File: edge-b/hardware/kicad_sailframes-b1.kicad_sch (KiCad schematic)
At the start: 79 parts, among them J1 Conn_01x15, J10 I2C_EXP1, J11 I2C_EXP2, J12 I2C_EXP3, J13 GPIO_EXP, J14 UART_DBG, J15 J_AUX, J16 GNSS_DBG, J17 LATCH_DBG, J2 JST_PH_BAT, J3 U.FL, J4 Conn_01x15, J5 MICROSD, J8 BNO085_DIRECT_SOLDER, J9 HOSYOND_3.5_TFT, U1 LC29HEAMD, U2 TP4056, U3 MT3608, U4 ESP32_DEVKIT_V1

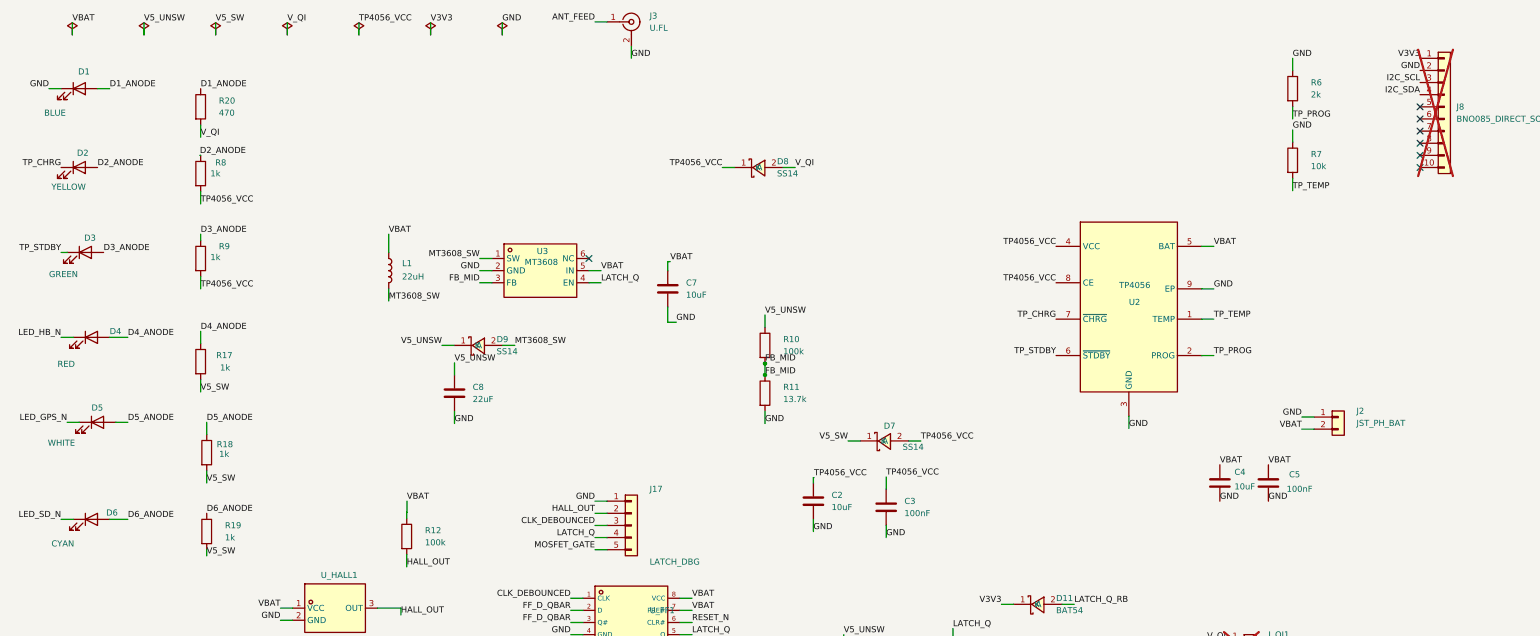
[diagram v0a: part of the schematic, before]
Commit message: B1: D6 cyan->blue, finalize JLC assembly BOM
- D6 LED cyan -> blue (C99290, same as D1) + filled its missing LCSC
- BOM finalized with tier-optimized parts (10k=C25804 Basic, TP4056=C16581,
  yellow=C89811, green=C99289, J1/J4=C2932676); deduped designators
  -> bom-jlcpcb-clean.csv (plugin had a duplicate-designator bug)
- NOTE: U_FF1 still C70285 (DCU) in schematic; correct part is
  SN74LVC1G74DCTR / SM8 = C840104 (fixed in JLC order, update schematic next)

Co-Authored-By: Claude Opus 4.8 (1M context) <noreply@anthropic.com>
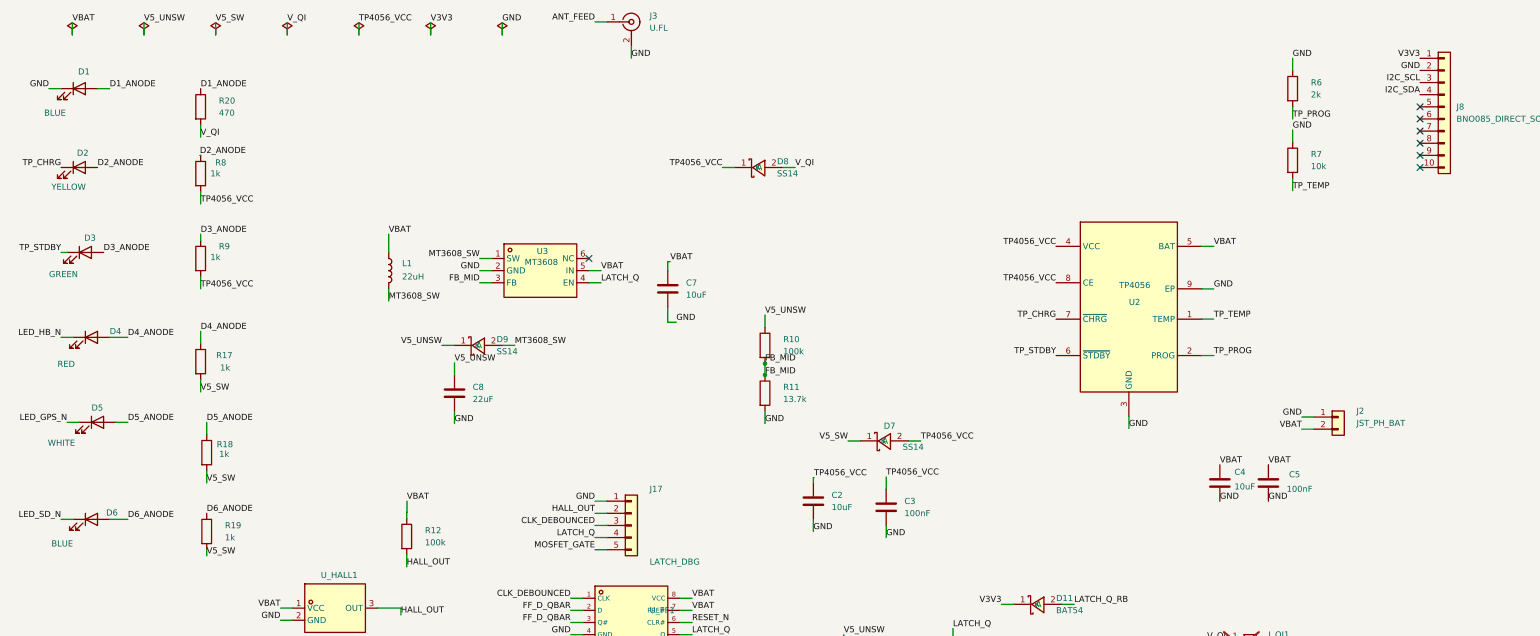
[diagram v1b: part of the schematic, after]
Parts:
- D6: value CYAN -> BLUE; LCSC Part # (none) -> C99290
- J8: now fitted; now in the parts list
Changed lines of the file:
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@@
 			)
 		)
-		(property "Value" "CYAN"
+		(property "Value" "BLUE"
 			(at 20.828 127 0)
 			(show_name no)
@@
 		(property "Description" ""
 			(at 29.21 121.92 0)
+			(hide yes)
+			(show_name no)
+			(do_not_autoplace no)
+			(effects
+				(font
+					(size 1.27 1.27)
+				)
+			)
+		)
+		(property "LCSC Part #" "C99290"
+			(at 20.828 127 0)
 			(hide yes)
 			(show_name no)
@@
 		(body_style 1)
 		(exclude_from_sim no)
-		(in_bom no)
+		(in_bom yes)
 		(on_board yes)
-		(in_pos_files no)
-		(dnp yes)
+		(in_pos_files yes)
+		(dnp no)
 		(fields_autoplaced yes)
 		(property "Reference" "J8"

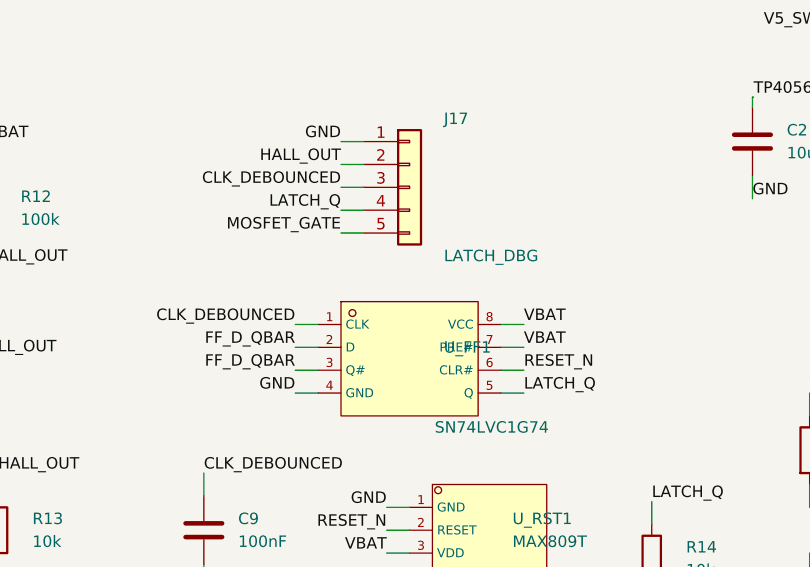
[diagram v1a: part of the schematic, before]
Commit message: edge-b/B1 hardware: KiCad PCB/schematic update + regenerated production files
- U_FF1 footprint swap: drop the mislabeled SM8 footprint and add the correct
  SN74LVC1G74 TSSOP8 footprint (C458768) to the B1_JLC library
- Updated kicad_sailframes-b1 PCB + schematic
- Regenerated production deliverables: gerbers zip, BOM, IPC netlist, CPL
  positions, and the JLCPCB fab BOM

Co-Authored-By: Claude Opus 4.8 (1M context) <noreply@anthropic.com>
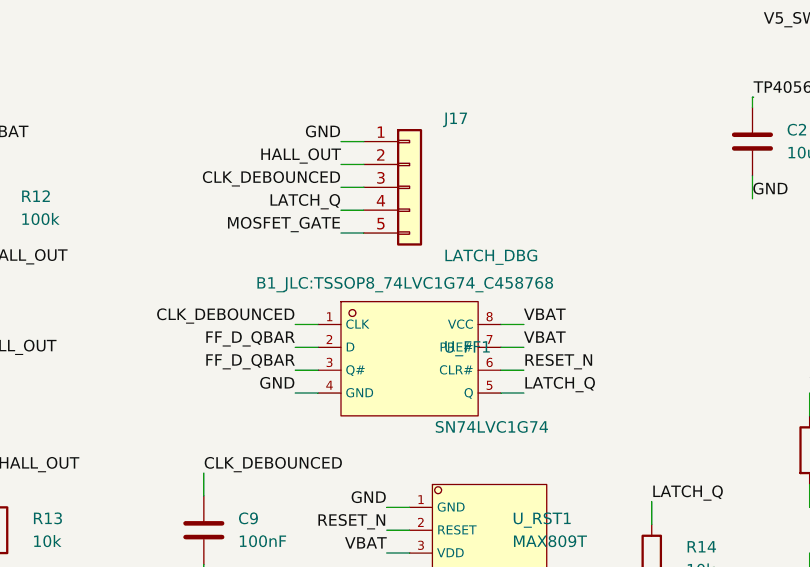
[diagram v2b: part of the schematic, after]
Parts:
- D2: LCSC Part # C125093 -> C89811
- D3: LCSC Part # C125093 -> C99289
- J1, J4: LCSC Part # (none) -> C2932676
- J10, J11, J12, J14, J16: LCSC Part # C2337 -> C5116483
- J13, J17: LCSC Part # C2337 -> C5156614
- J15: LCSC Part # C2337 -> C32713272
- J8: LCSC Part # (none) -> C57369
- J9: LCSC Part # C2337 -> C57369
- R13, R14, R16, R23, R24, R25, R26, R27, R28, R7: LCSC Part # C15401 -> C25804
- U2: LCSC Part # C382139 -> C16581
- U_FF1: footprint B1_JLC:VSSOP-8_DCU_2.3x2mm_P0.65mm -> B1_JLC:TSSOP8_74LVC1G74_C458768; LCSC Part # C70285 -> C458768
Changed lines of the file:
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@@
 			)
 		)
-		(property "LCSC Part #" "C2337"
+		(property "LCSC Part #" "C5116483"
 			(at 0 0 0)
 			(hide yes)
@@
 			)
 		)
-		(property "LCSC Part #" "C2337"
+		(property "LCSC Part #" "C5156614"
 			(at -107.76 -96.81 0)
 			(hide yes)
@@
 			)
 		)
-		(property "LCSC Part #" "C15401"
+		(property "LCSC Part #" "C25804"
 			(at 0 0 0)
 			(hide yes)
@@
 			)
 		)
-		(property "LCSC Part #" "C2337"
+		(property "LCSC Part #" "C57369"
 			(at 0 0 0)
 			(hide yes)
@@
 			)
 		)
-		(property "LCSC Part #" "C125093"
+		(property "LCSC Part #" "C89811"
 			(at -188.54 -37.24 0)
 			(hide yes)
@@
 			)
 		)
+		(property "LCSC Part #" "C2932676"
+			(at 351.79 114.3 0)
+			(hide yes)
+			(show_name no)
+			(do_not_autoplace no)
+			(effects
+				(font
+					(size 1.27 1.27)
+				)
+			)
+		)
 		(property "Datasheet" ""
 			(at 351.79 114.3 0)
@@
 			)
 		)
-		(property "LCSC Part #" "C15401"
+		(property "LCSC Part #" "C25804"
 			(at 0 0 0)
 			(hide yes)
@@
 			)
 		)
-		(property "LCSC Part #" "C2337"
+		(property "LCSC Part #" "C5116483"
 			(at 0 0 0)
 			(hide yes)
@@
 			)
 		)
-		(property "LCSC Part #" "C2337"
+		(property "LCSC Part #" "C5116483"
 			(at 46.99 78.74 0)
 			(hide yes)
@@
 			)
 		)
-		(property "LCSC Part #" "C15401"
+		(property "LCSC Part #" "C25804"
 			(at 0 0 0)
 			(hide yes)
@@
 			)
 		)
-		(property "LCSC Part #" "C15401"
+		(property "LCSC Part #" "C25804"
 			(at 0 0 0)
 			(hide yes)
@@
 			)
 		)
-		(property "Footprint" "B1_JLC:VSSOP-8_DCU_2.3x2mm_P0.65mm"
-			(at 142.24 142.24 0)
-			(hide yes)
+		(property "Footprint" "B1_JLC:TSSOP8_74LVC1G74_C458768"
+			(at 141.732 133.858 0)
 			(show_name no)
 			(do_not_autoplace no)
@@
 			)
 		)
-		(property "LCSC Part #" "C70285"
+		(property "LCSC Part #" "C458768"
 			(at 2.03 1.74 0)
 			(hide yes)
@@
 			)
 		)
-		(property "LCSC Part #" "C15401"
+		(property "LCSC Part #" "C25804"
 			(at 0 0 0)
 			(hide yes)
@@
 			)
 		)
-		(property "LCSC Part #" "C382139"
+		(property "LCSC Part #" "C16581"
 			(at 6.35 -5.08 0)
 			(hide yes)
@@
 			)
 		)
-		(property "LCSC Part #" "C2337"
+		(property "LCSC Part #" "C5116483"
 			(at 46.99 78.74 0)
 			(hide yes)
@@
 			)
 		)
+		(property "LCSC Part #" "C2932676"
+			(at 393.7 114.3 0)
+			(hide yes)
+			(show_name no)
+			(do_not_autoplace no)
+			(effects
+				(font
+					(size 1.27 1.27)
+				)
+			)
+		)
 		(property "Datasheet" ""
 			(at 393.7 114.3 0)
@@
 			)
 		)
-		(property "LCSC Part #" "C2337"
+		(property "LCSC Part #" "C32713272"
 			(at 0 0 0)
 			(hide yes)
@@
 			)
 		)
+		(property "LCSC Part #" "C57369"
+			(at 312.42 35.56 0)
+			(hide yes)
+			(show_name no)
+			(do_not_autoplace no)
+			(effects
+				(font
+					(size 1.27 1.27)
+				)
+			)
+		)
 		(property "Datasheet" ""
 			(at 312.42 35.56 0)
@@
 			)
 		)
-		(property "LCSC Part #" "C15401"
+		(property "LCSC Part #" "C25804"
 			(at 0 0 0)
 			(hide yes)
@@
 			)
 		)
-		(property "LCSC Part #" "C2337"
+		(property "LCSC Part #" "C5156614"
 			(at 46.99 78.74 0)
 			(hide yes)
@@
 			)
 		)
-		(property "LCSC Part #" "C15401"
+		(property "LCSC Part #" "C25804"
 			(at 0 0 0)
 			(hide yes)
@@
 			)
 		)
-		(property "LCSC Part #" "C15401"
+		(property "LCSC Part #" "C25804"
 			(at 10.46 -43.75 0)
 			(hide yes)
@@
 			)
 		)
-		(property "LCSC Part #" "C15401"
+		(property "LCSC Part #" "C25804"
 			(at 0 0 0)
 			(hide yes)
@@
 			)
 		)
-		(property "LCSC Part #" "C15401"
+		(property "LCSC Part #" "C25804"
 			(at 0 0 0)
 			(hide yes)
@@
 			)
 		)
-		(property "LCSC Part #" "C125093"
+		(property "LCSC Part #" "C99289"
 			(at -187.27 -4.46 0)
 			(hide yes)
@@
 			)
 		)
-		(property "LCSC Part #" "C2337"
+		(property "LCSC Part #" "C5116483"
 			(at 0 0 0)
 			(hide yes)

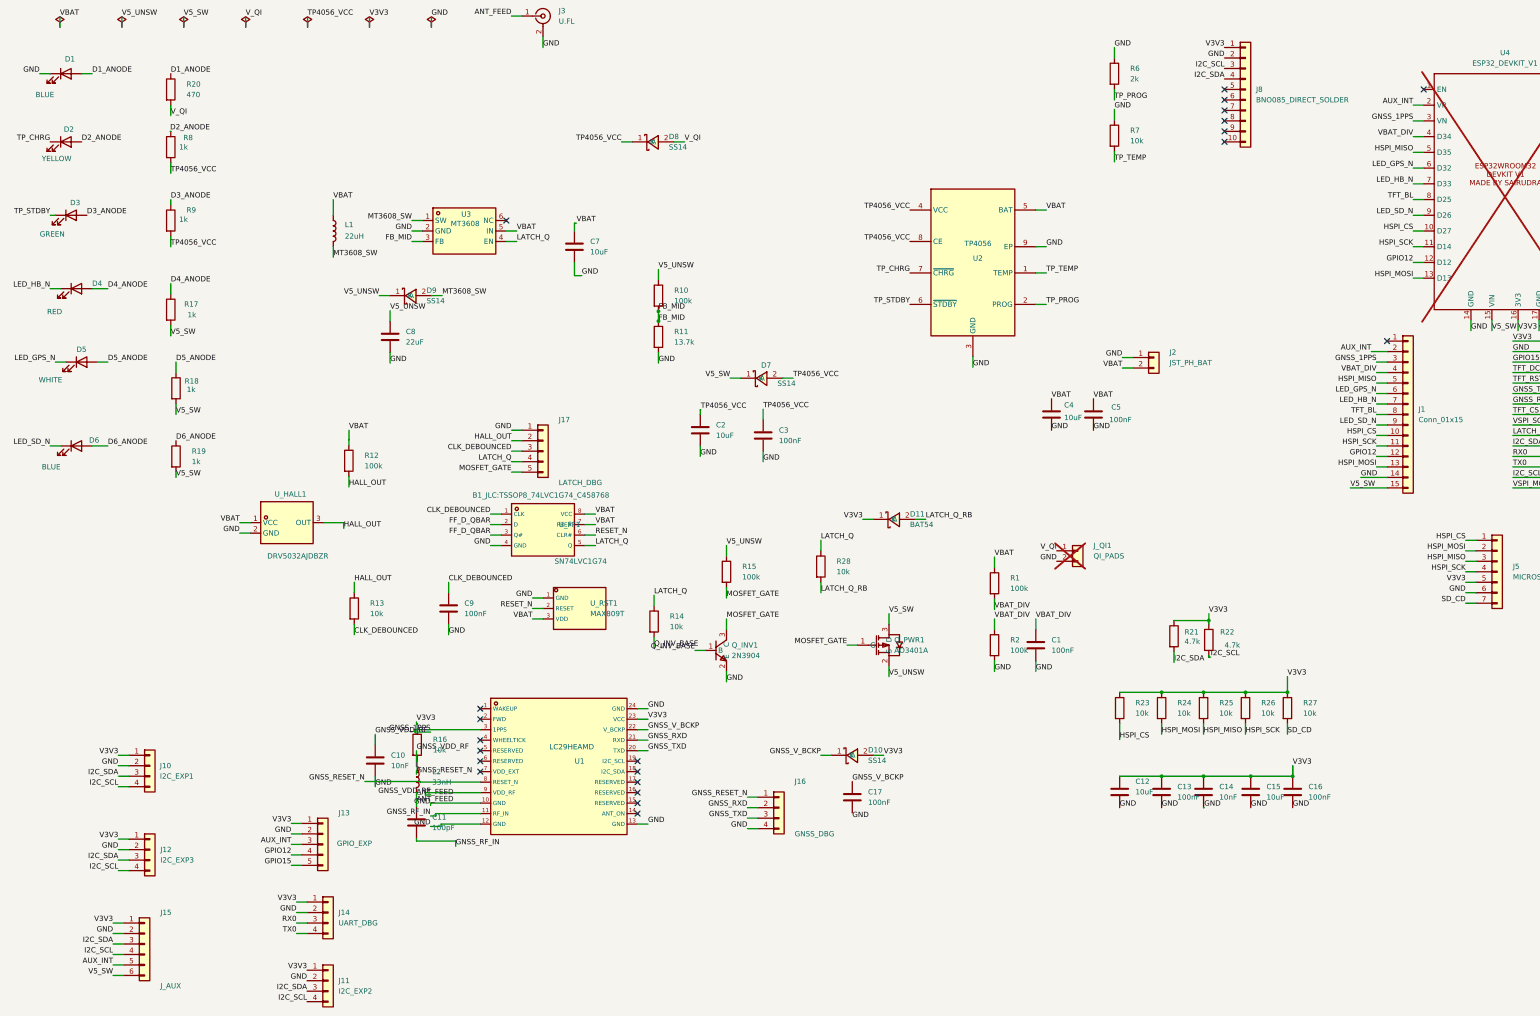
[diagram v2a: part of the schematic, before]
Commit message: B1 v0.13: Qi-pad on/off + J5 microSD fix + antenna keepout
Three build-gating fixes for the 30-unit B1 respin, all netlist-verified
(not just DRC-clean — the v0.12 bugs were DRC-clean):

On/off → Qi pad (magnet AND button removed, zero enclosure penetration):
- Delete the magnetic-latch front end: U_HALL1 (DRV5032), U_FF1
  (SN74LVC1G74 FF), U_RST1 (MAX809), R12/R13/C9 debounce, D11 clamp.
- PWR_HOLD = GPIO19 now drives /LATCH_Q through the pre-existing R28
  (value 10k -> 0R so boost EN sees a full 3.3V, not the ~1.9V divider).
  The MCU now holds AND releases its own power.
- Add R30 100k pulldown (default-off), R31/R32 47k/68k V_QI divider ->
  GPIO15 (QI_PRESENT, on-pad ~2.96V). Charge-complete inferred from the
  existing GPIO34 VBAT ADC.
- J17 repurposed to a v0.13 power-debug header (GPIO15/V_QI/LATCH_Q/
  MOSFET_GATE).

J5 microSD pinout fix (was dead on every v0.12 board):
- Correct net->pad: CS->pad2, MOSI->pad3, VDD->pad4, SCK->pad5, GND->pad6,
  MISO->pad7 (card now gets power + clock on the right contacts).
- Drop unused SD_CD (firmware detects via SD.begin/cardType) + delete its
  pull-up R27.

Antenna: ground-pour keepout added under the DevKit antenna (Option 1;
notch/overhang + E1 bench validation still TODO before fab).

Firmware (PWR_HOLD on boot, lift-to-race, charge-complete/low-batt auto-off)
is spec-only in B1_V013_QI_POWER.md, not yet written. Do not fab until the
firmware + antenna overhang + fab-output regen are done.

Co-Authored-By: Claude Opus 4.8 (1M context) <noreply@anthropic.com>
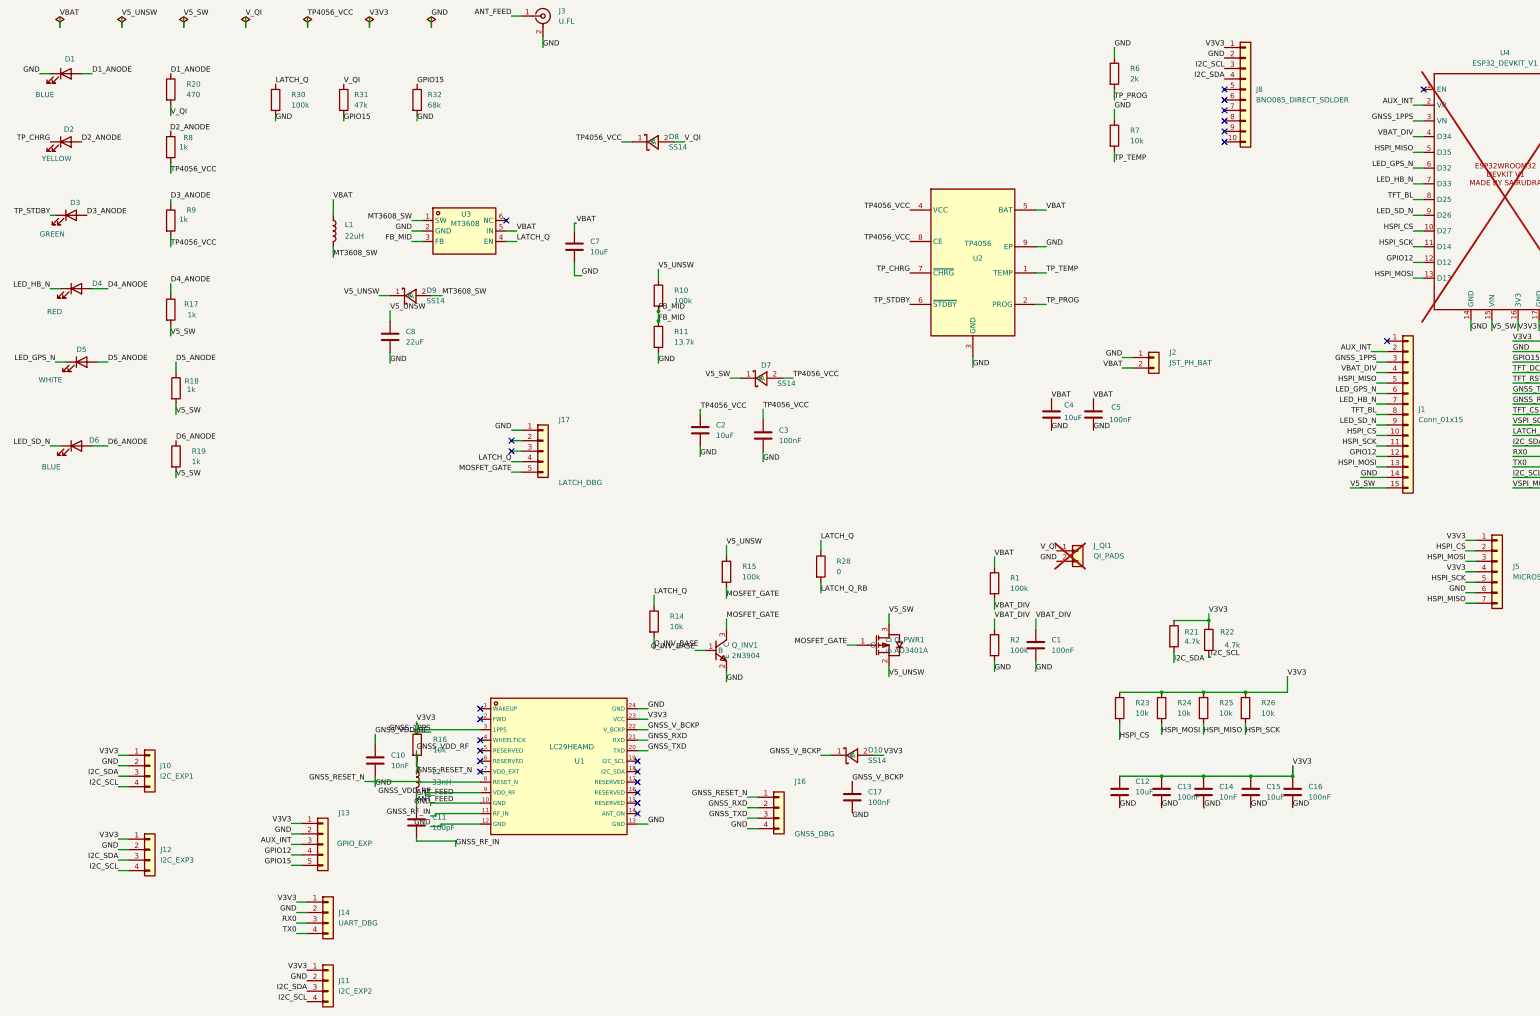
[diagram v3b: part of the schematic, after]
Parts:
- removed C9: 100nF, Capacitor_SMD:C_0603_1608Metric, symbol Device:C
- removed D11: BAT54, Diode_SMD:D_SOD-323, symbol B1_SS14:SS14
- removed J15: J_AUX, Connector_PinHeader_2.54mm:PinHeader_1x06_P2.54mm_Vertical, symbol Connector_Generic:Conn_01x06
- removed R12: 100k, Resistor_SMD:R_0603_1608Metric, symbol Device:R
- removed R13, R27: 10k, Resistor_SMD:R_0603_1608Metric, symbol Device:R
- removed U_FF1: SN74LVC1G74, B1_JLC:TSSOP8_74LVC1G74_C458768, symbol B1_JLC:SN74LVC1G74DCTR
- removed U_HALL1: DRV5032AJDBZR, Package_TO_SOT_SMD:SOT-23, symbol B1_DRV5032AJ:DRV5032AJDMRR
- removed U_RST1: MAX809T, Package_TO_SOT_SMD:SOT-23, symbol B1_JLC:MAX809T
- added R30: 100k, Resistor_SMD:R_0603_1608Metric, symbol Device:R
- added R31: 47k, Resistor_SMD:R_0603_1608Metric, symbol Device:R
- added R32: 68k, Resistor_SMD:R_0603_1608Metric, symbol Device:R
- R28: value 10k -> 0; LCSC Part # C25804 -> C17168
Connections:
- net SD_CD is gone; now on net HSPI_MISO: J5.7 (Pin_7)
- net GND: now also R30.2, R32.2
- net GPIO15: now also R31.2, R32.1
- net HSPI_CS: now also J5.2 (Pin_2); no longer J5.1 (Pin_1)
- net HSPI_MISO: no longer J5.3 (Pin_3)
- net HSPI_MOSI: now also J5.3 (Pin_3); no longer J5.2 (Pin_2)
- net HSPI_SCK: now also J5.5 (Pin_5); no longer J5.4 (Pin_4)
- net LATCH_Q: now also R30.1
- net V3V3: now also J5.1 (Pin_1), J5.4 (Pin_4); no longer J5.5 (Pin_5)
- net V_QI: now also R31.1
- net CLK_DEBOUNCED: no longer names the net of J17.3 (Pin_3)
- net HALL_OUT: no longer names the net of J17.2 (Pin_2)
- no-connect marks 23 -> 25
